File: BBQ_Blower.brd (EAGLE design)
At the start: 95.9 x 84.8 mm, 31 parts, among them IC1 MAX31855RASA+, IC2 MAX31855RASA+, IC3 MAX31855RASA+, J1 1X2-3.5MM, J10 1X2-3.5MM, J11 1X2-3.5MM, J2 1X2-3.5MM, J3 PCC-SMP-K-100-R-ROHS, J4 PCC-SMP-K-100-R-ROHS, J5 1X2-3.5MM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

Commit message: initial
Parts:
- removed J1, J10, J11, J2, J5, J6, J7, J9: 1X2-3.5MM, adafruit:1X2-3.5MM
- added M1, M2, PWR, RL1, RL2, TH1: (no value), SparkFun-Connectors:SCREWTERMINAL-5MM-2
- added SV1: (no value), con-lstb:MA03-2
- moved C4 72.9 mm to (70.1, 60.2), turned to 0 degrees
- moved JP1 65.4 mm to (86.4, 48.8), turned to 90 degrees
- moved IC3 57.8 mm to (69.8, 37.3), turned to 0 degrees
- moved IC1 55.8 mm to (70.1, 66.5), turned to 0 degrees
- moved C2 54.2 mm to (69.8, 31.0), turned to 0 degrees
- moved IC2 54.1 mm to (70.1, 50.3), turned to 0 degrees
- moved U1 50.5 mm to (69.3, 49.0), turned to 180 degrees
- moved K1 46.5 mm to (25.9, 68.1), turned to 270 degrees
- moved C3 44.0 mm to (30.7, 74.7)
- moved K2 42.1 mm to (26.2, 41.4), turned to 270 degrees
- moved C1 37.3 mm to (70.1, 44.2), turned to 0 degrees
- moved D3 34.0 mm to (49.0, 41.7), turned to 270 degrees
- moved D1 30.3 mm to (47.8, 70.1)
- moved D2 30.0 mm to (51.1, 70.1)
- moved D4 28.9 mm to (52.6, 41.7), turned to 270 degrees
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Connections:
- removed net CMD: JP1.5, U1.7
- removed net D0: JP1.6, U1.8
- new net MISO: JP1.6, SV1.1, U1.8
- new net MOSI: JP1.5, SV1.4, U1.7
- net 3V3: now also SV1.6
- net BLOWER1: now also M2.1; no longer J6.1
- net BLOWER2: now also M1.1; no longer J5.1
- net CLK: now also SV1.3
- net GND: now also PWR.1, SV1.2; no longer J7.1
- net RELAY1(+): now also RL2.1; no longer J1.2
- net RELAY1(-): now also RL2.2; no longer J1.1
- net RELAY2(+): now also RL1.1; no longer J2.2
- net RELAY2(-): now also RL1.2; no longer J2.1
- net RST: now also SV1.5
- net T1+: no longer J9.1
- net T1-: no longer J9.2
- net T2+: no longer J10.1
- net T2-: no longer J10.2
- net T3+: now also TH1.1; no longer J11.1
- net T3-: now also TH1.2; no longer J11.2
- net VDD: now also M1.2, M2.2, PWR.2; no longer J5.2, J6.2, J7.2
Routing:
- net MOSI: track 0.00 -> 46.6 mm
- net D0: track 45.7 -> 0.00 mm
- net T3+: track 90.3 -> 45.3 mm
- net T3-: track 88.7 -> 47.8 mm, vias 0 -> 2
- net CMD: track 40.3 -> 0.00 mm
- net MISO: track 0.00 -> 39.7 mm
- net T2-: track 81.9 -> 121.3 mm, vias 0 -> 1
- net EN: track 48.8 -> 10.1 mm
- net VDD: track 237.2 -> 203.9 mm, vias 2 -> 0
- net 3V3: track 120.4 -> 153.4 mm
- net T2+: track 87.6 -> 56.4 mm, vias 0 -> 1
- net BLOWER_1: track 8.24 -> 37.7 mm
- net SCK: track 71.7 -> 42.8 mm, vias 0 -> 1
- net D1: track 34.9 -> 6.22 mm
- net GND: track 30.0 -> 2.03 mm, vias 10 -> 2
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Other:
- board size 95.9 x 84.8 mm -> 84.9 x 75.9 mm
- board text added: "Board: BBQ Controller Author: Cody Fischer Date: November 2018 Rev: 1.0"
- board text added: "GND"
- board text added: "M1+"
- board text added: "M1-"
- board text added: "M2+"
- board text added: "M2-"
- board text added: "RL2+"
- board text added: "RL2-"
- board text added: "VDD"

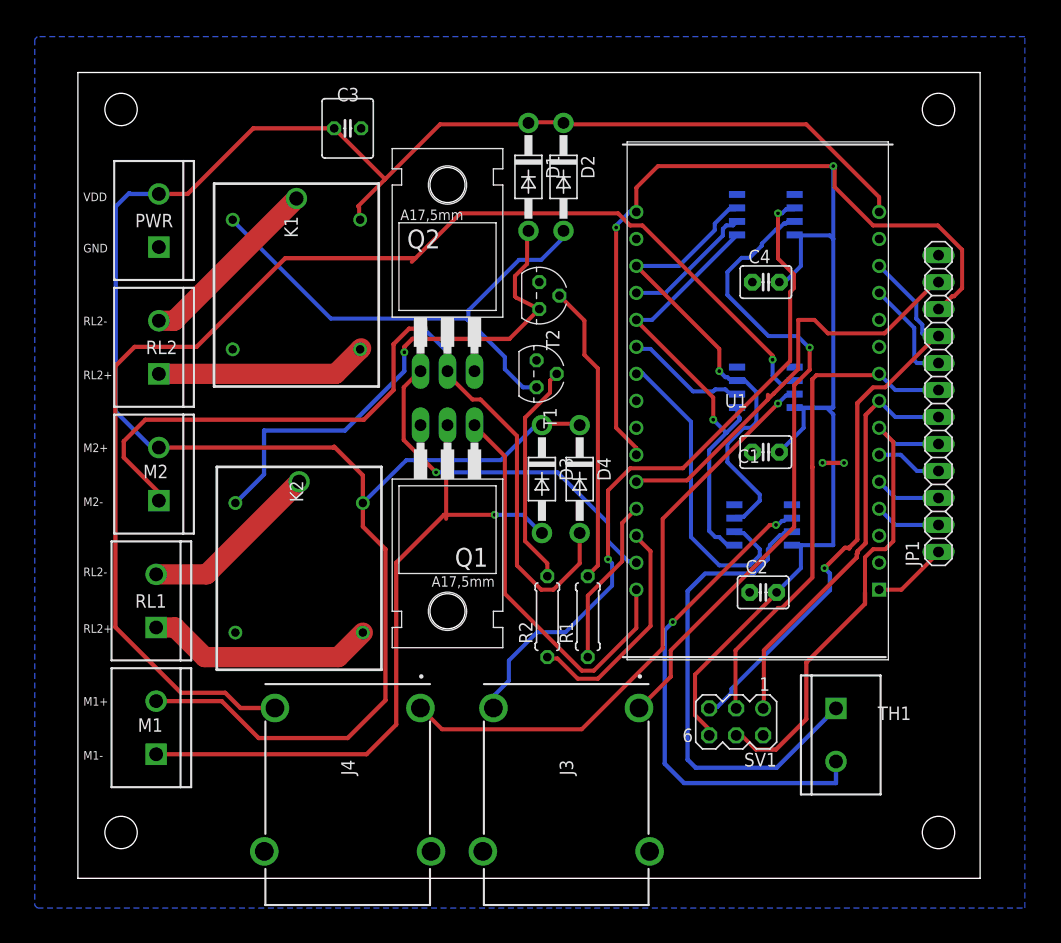
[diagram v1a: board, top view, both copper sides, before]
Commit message: added Lora Component
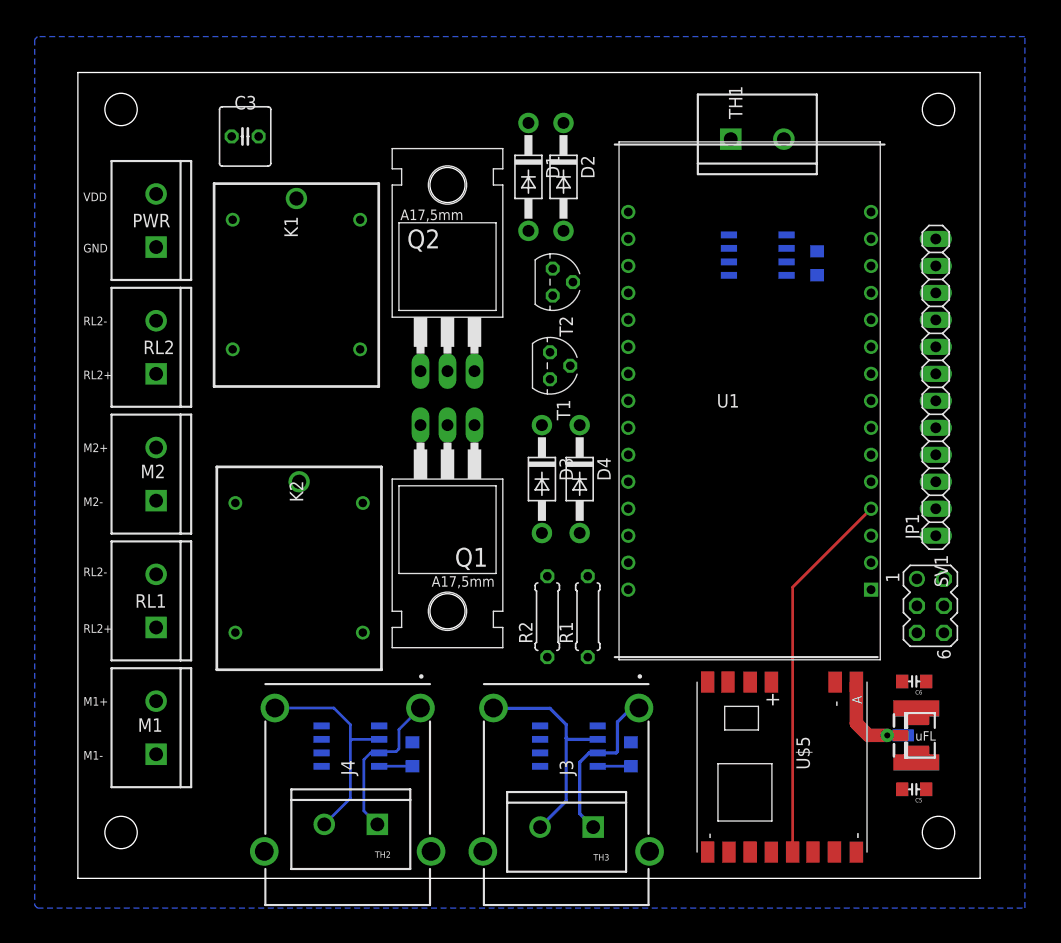
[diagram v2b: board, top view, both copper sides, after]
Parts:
- removed C4: (no value), capacitor-wima:C2.5-3
- added C5: 10uF, _c2h:0805-CAP-LARGEPADS
- added C6, C7: 1uF, _c2h:0805-CAP-LARGEPADS
- added J$2: ANTENNATINY, _c2h:SMA_UFL_PAD_TINY
- added TH2, TH3: (no value), SparkFun-Connectors:SCREWTERMINAL-5MM-2
- added U$5: RFM95, _c2h:RFM95
- C1, C2: value (none) -> 1uF; device capacitor-wima:C2.5-3 -> _c2h:0805-CAP-LARGEPADS
- moved TH1 54.5 mm to (66.8, 73.7), turned to 0 degrees
- moved IC1 53.4 mm to (51.6, 16.5)
- moved IC2 51.7 mm to (31.0, 16.5)
- moved C2 36.4 mm to (36.8, 15.7), flipped to the bottom, turned to 270 degrees
- moved C1 31.2 mm to (57.4, 15.7), flipped to the bottom, turned to 270 degrees
- moved IC3 25.4 mm to (69.3, 62.7)
- moved SV1 21.3 mm to (85.6, 29.7), turned to 270 degrees
- moved C3 9.68 mm to (21.1, 73.9)
- moved T2 1.80 mm to (50.0, 60.2)
- moved JP1 1.55 mm to (86.1, 50.3)
- moved T1 1.48 mm to (49.8, 52.3)
- moved U1 0.76 mm to (68.6, 49.0)
- moved M2 0.25 mm to (12.7, 39.6)
- moved PWR 0.25 mm to (12.7, 63.5)
- moved RL2 0.25 mm to (12.7, 51.6)
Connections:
- new net ANT: J$2.ANT1, J$2.ANT2, J$2.ANT3, U$5.ANT
- new net CS_LORA: U$5.NSS, U1.4
- new net DIO0: U$5.DIO0
- new net DIO1: U$5.DIO1
- new net DIO2: U$5.DIO2
- new net GPIO12: U$5.MISO
- new net GPIO13: U$5.MOSI
- new net GPIO14: U$5.SCK
- net 3V3: now also C5.2, C6.2, C7.2, U$5.VDD; no longer C4.2
- net D3: no longer U1.4
- net GND: now also C5.1, C6.1, C7.1, J$2.GND1, J$2.GND2, J$2.GND3, J$2.GND4, U$5.GND, U$5.GND1, U$5.GND2; no longer C4.1
- net RST: now also U$5.RST
- net T1+: now also TH3.1
- net T1-: now also TH3.2
- net T2+: now also TH2.1
- net T2-: now also TH2.2
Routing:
- net VDD: track 203.9 -> 0.00 mm
- net 3V3: track 153.4 -> 6.27 mm, vias 2 -> 0
- net T2-: track 121.3 -> 20.9 mm, vias 1 -> 0
- net BLOWER1: track 79.7 -> 0.00 mm, vias 1 -> 0
- net BLOWER2: track 64.2 -> 0.00 mm, vias 1 -> 0
- net RST: track 55.8 -> 0.00 mm, vias 1 -> 0
- net N$2: track 49.2 -> 0.00 mm, vias 1 -> 0
- net N$8: track 49.2 -> 0.00 mm
- net T3-: track 47.8 -> 0.00 mm, vias 2 -> 0
- net CLK: track 47.0 -> 0.00 mm
- net MOSI: track 46.6 -> 0.00 mm
- net SO: track 45.8 -> 0.00 mm, vias 1 -> 0
- net T3+: track 45.3 -> 0.00 mm
- net T1+: track 61.1 -> 16.0 mm, vias 1 -> 0
- net T1-: track 65.7 -> 21.2 mm, vias 2 -> 0
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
